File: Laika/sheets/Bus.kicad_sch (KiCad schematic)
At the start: 0 parts

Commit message: Added breakout for I2C as external bus
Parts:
- added J10: Conn_01x04, symbol Connector_Generic:Conn_01x04
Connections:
- new net +1V8: J10.1 (Pin_1)
- new net EXT_BUS_I2C_SCL: J10.4 (Pin_4)
- new net EXT_BUS_I2C_SDA: J10.3 (Pin_3)
- new net GND: J10.2 (Pin_2)
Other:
- note added: "External Bus"
- note added: "I2C"

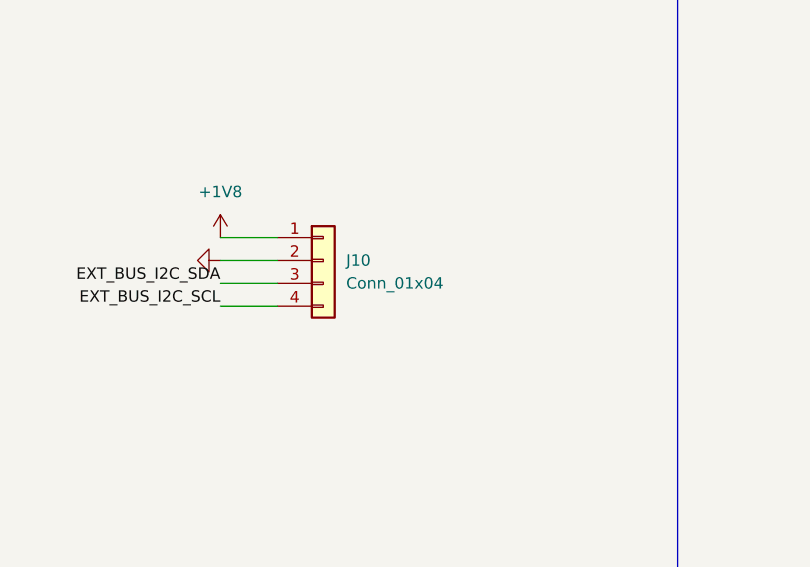
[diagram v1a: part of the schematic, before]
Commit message: Populated BOM with part numbers and footprints
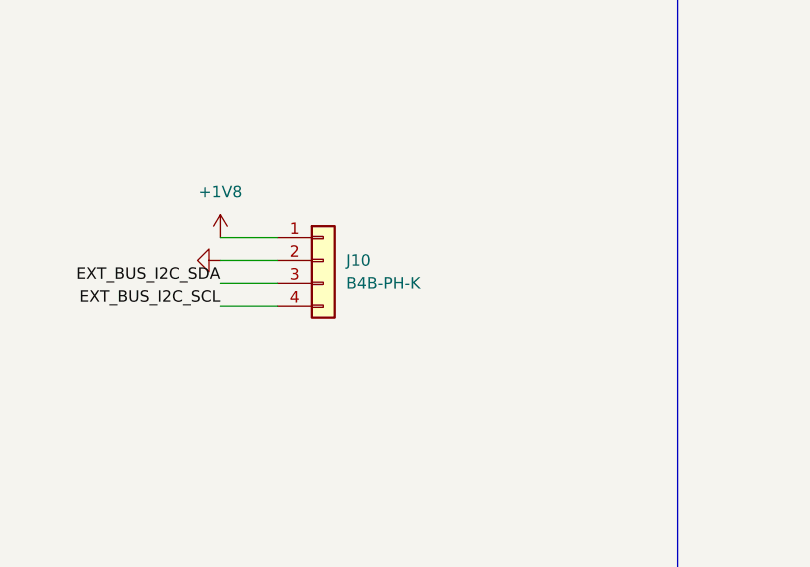
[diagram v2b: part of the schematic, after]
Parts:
- J10: value Conn_01x04 -> B4B-PH-K; footprint (none) -> Connector_JST:JST_PH_B4B-PH-K_1x04_P2.00mm_Vertical; JLC Part Type (none) -> Extended; Manafacturer (none) -> JST Commercial; Part Number (none) -> B4B-PH-K
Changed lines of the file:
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@@
 			)
 		)
-		(property "Value" "Conn_01x04"
+		(property "Value" "B4B-PH-K"
 			(at 139.7 95.2499 0)
 			(effects
@@
 			)
 		)
-		(property "Footprint" ""
+		(property "Footprint" "Connector_JST:JST_PH_B4B-PH-K_1x04_P2.00mm_Vertical"
 			(at 137.16 92.71 0)
 			(effects
@@
 			)
 		)
-		(property "Datasheet" "~"
+		(property "Datasheet" "https://www.jst-mfg.com/product/pdf/eng/ePH.pdf"
 			(at 137.16 92.71 0)
 			(effects
@@
 			(at 137.16 92.71 0)
 			(effects
+				(font
+					(size 1.27 1.27)
+				)
+				(hide yes)
+			)
+		)
+		(property "JLC Part Type" "Extended"
+			(at 137.16 92.71 0)
+			(effects
+				(font
+					(size 1.27 1.27)
+				)
+				(hide yes)
+			)
+		)
+		(property "Manafacturer" "JST Commercial "
+			(at 137.16 92.71 0)
+			(effects
+				(font
+					(size 1.27 1.27)
+				)
+				(hide yes)
+			)
+		)
+		(property "Part Number" "B4B-PH-K "
+			(at 137.16 92.71 0)
+			(effects
